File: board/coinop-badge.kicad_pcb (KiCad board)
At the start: 2 copper layers, 90 x 96 mm, 40 parts, among them CON1 AVR-ISP-6, J1 Conn_01x02, SW1 SW_Push, SW2 SW_Push, U1 ATMEGA48A-AU

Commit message: Removed erroneous connection left over from larger charlieplex array
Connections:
- RN2 pad 2: CHARLIE-4 -> Net-(RN2-Pad2)
- U1 pad 30: CHARLIE-4 -> Net-(U1-Pad30)
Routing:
- net CHARLIE-4: track 9.05 -> 0.00 mm

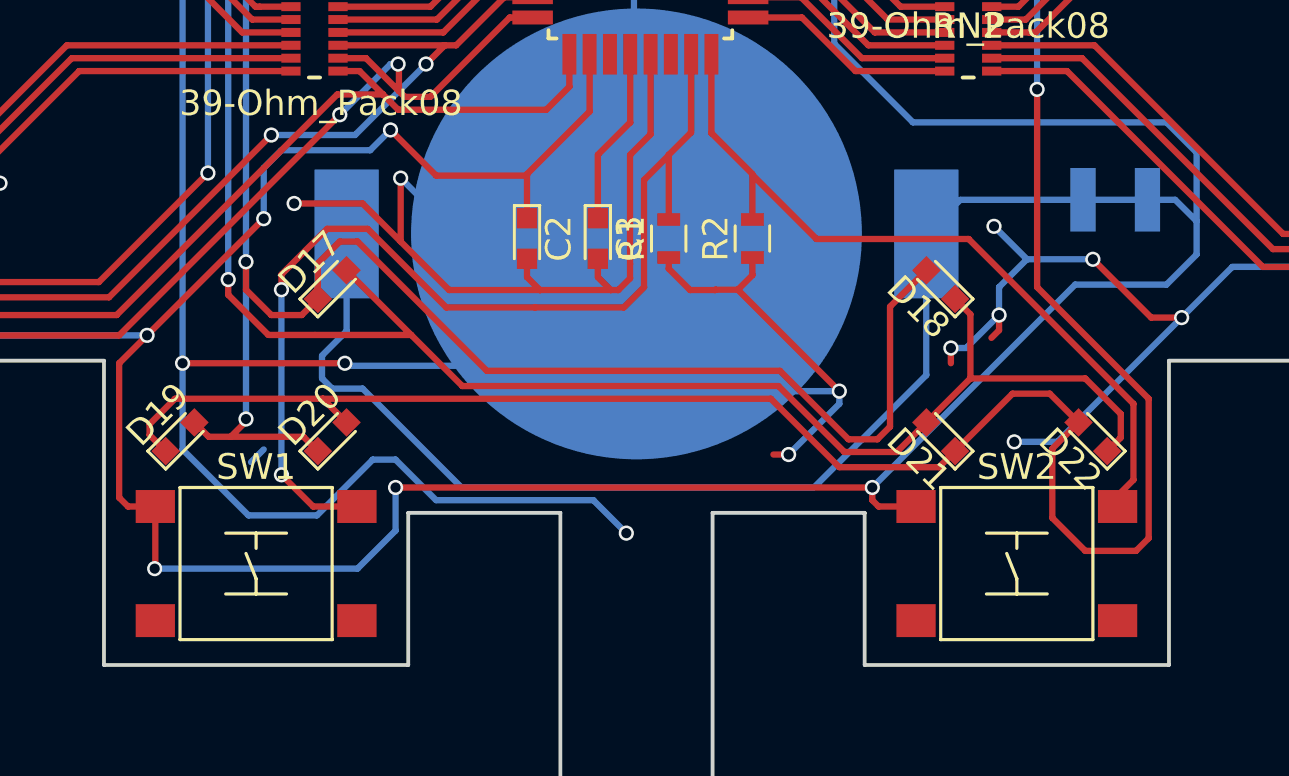
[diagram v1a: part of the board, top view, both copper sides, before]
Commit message: Fixed routing mistake on buttons. Board now at v2
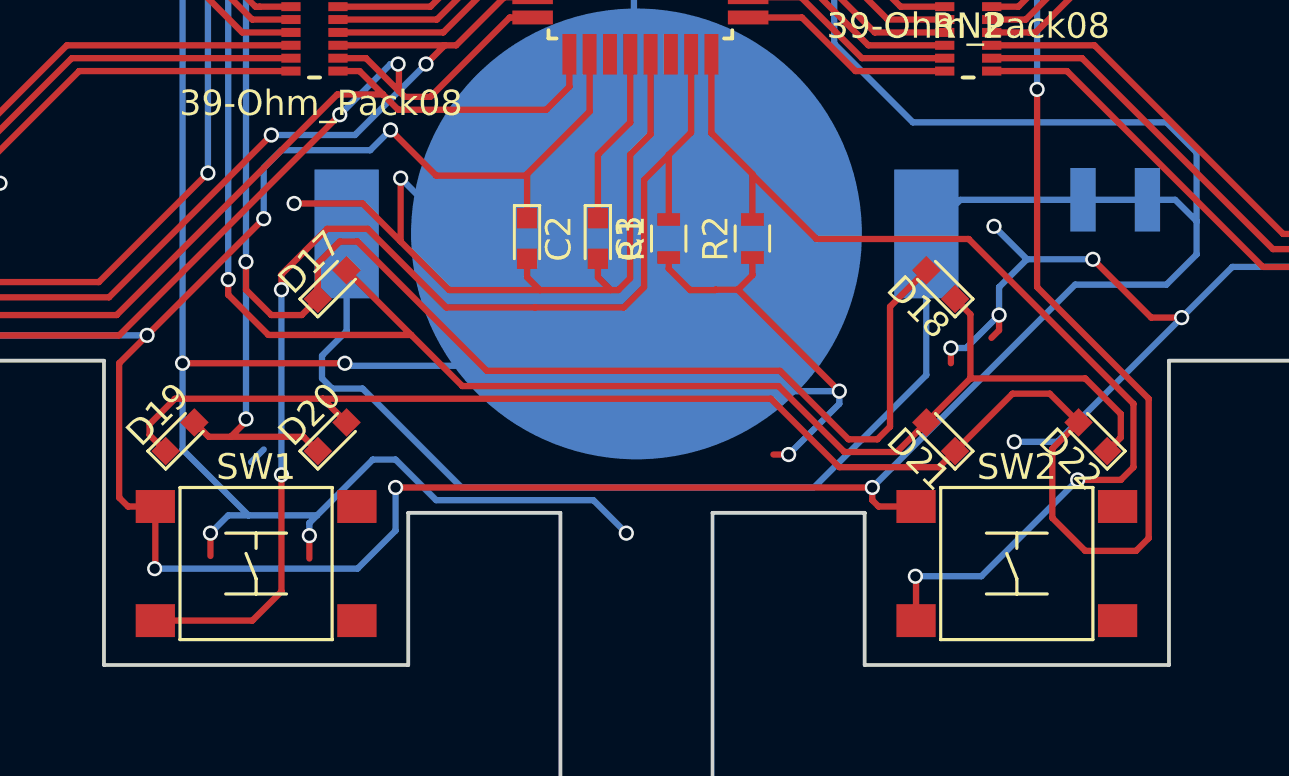
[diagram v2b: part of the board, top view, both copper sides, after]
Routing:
- net SW-SELECT: track 30.3 -> 40.6 mm, vias 0 -> 2
- net SW-POWER: track 40.5 -> 47.1 mm
- net GND: track 498.5 -> 503.0 mm, vias 32 -> 34

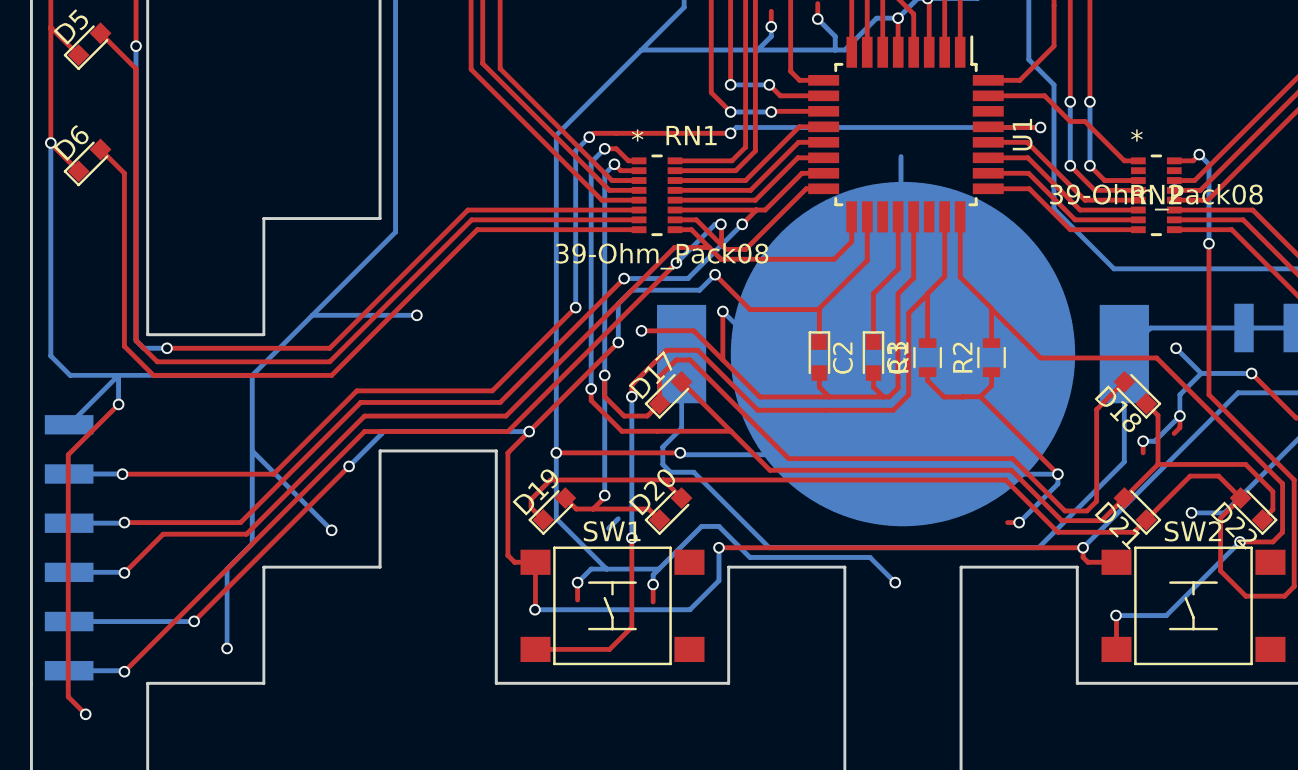
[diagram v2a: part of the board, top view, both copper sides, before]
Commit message: Fixed button routing error Added SAO header (wired as add-on, not host) Added button labels
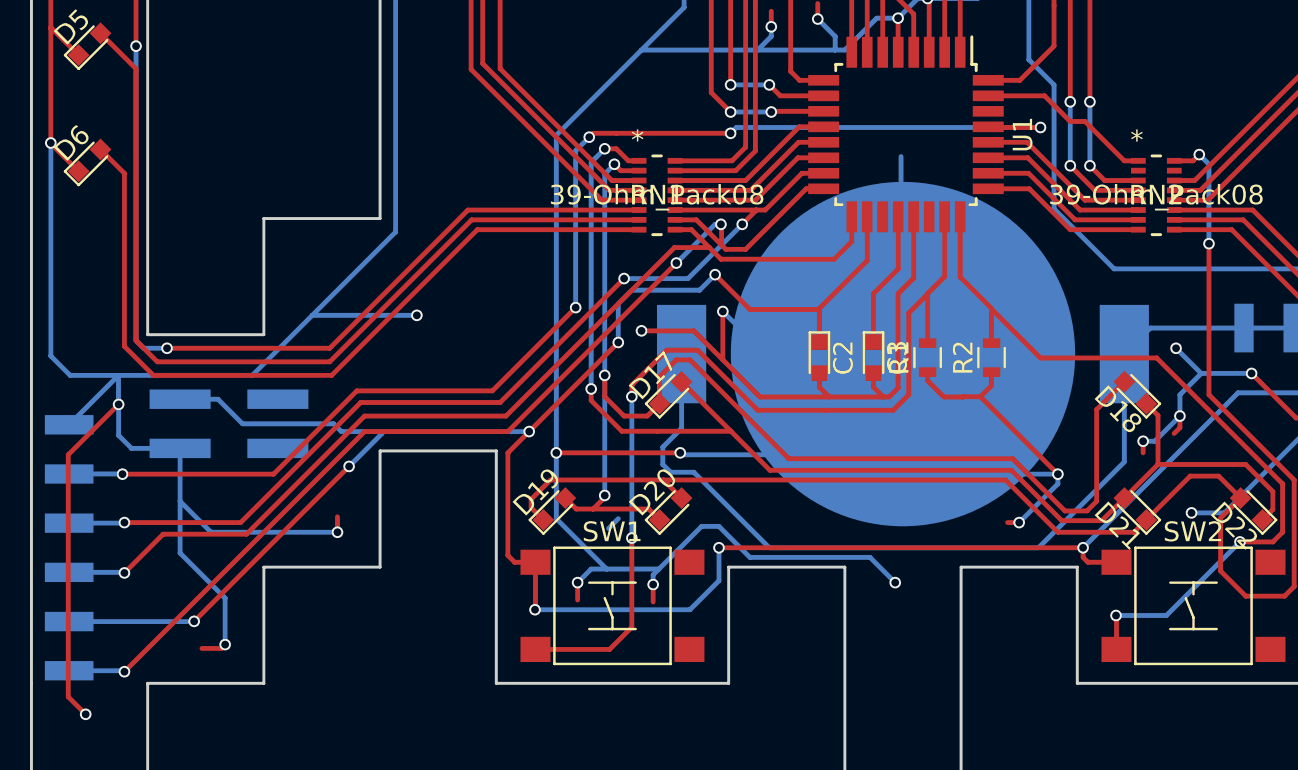
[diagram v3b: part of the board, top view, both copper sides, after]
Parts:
- added G***: LOGO, Szczys:LOGO-disco, B.Cu at (168.0, 132.0)
- added G***: LOGO, Szczys:LOGO-juice, B.Cu at (138.0, 132.0)
- added J2: Conn_02x02_Odd_Even, Szczys:SAO_Pin_Header_Straight_2x02_Pitch2.54mm_SMD, B.Cu at (118.2, 124.6)
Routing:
- net VCC: track 218.9 -> 230.1 mm
- net GND: track 503.0 -> 509.6 mm
